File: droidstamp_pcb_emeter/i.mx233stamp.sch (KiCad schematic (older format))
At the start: 0 parts

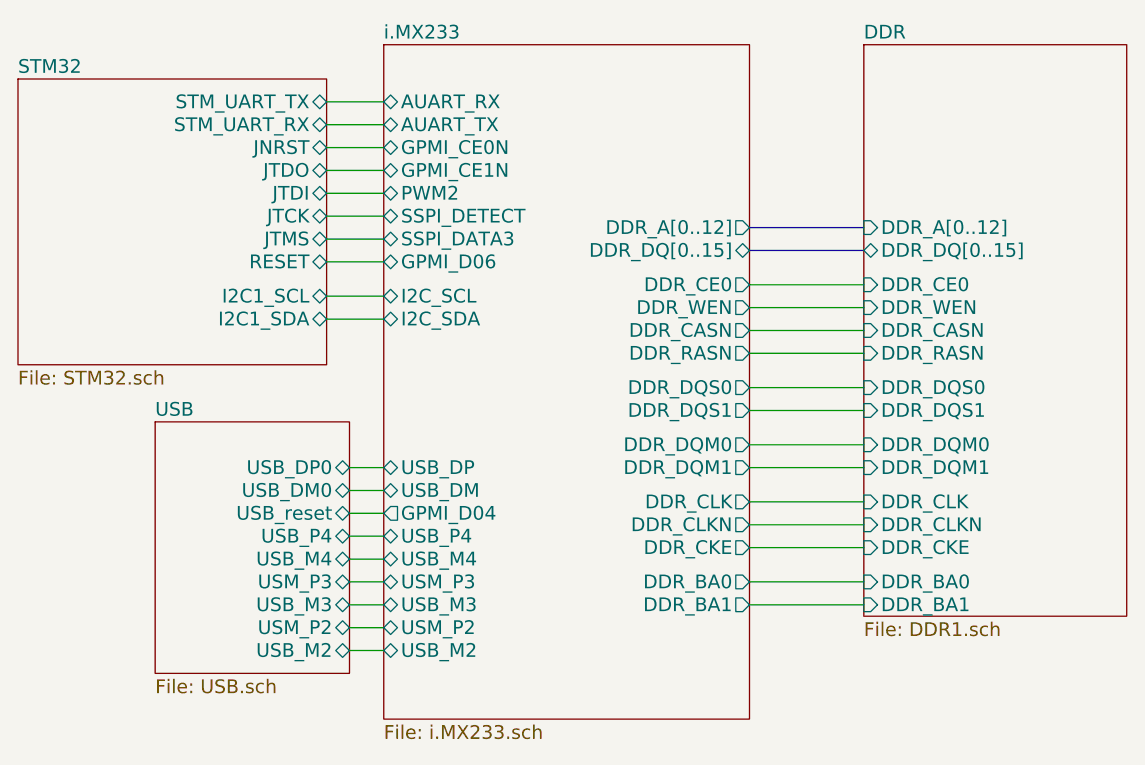
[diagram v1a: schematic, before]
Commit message: Adición de la linea BOOT_MODE para modificar el inicio del stm32 desde memoria interna o jtag
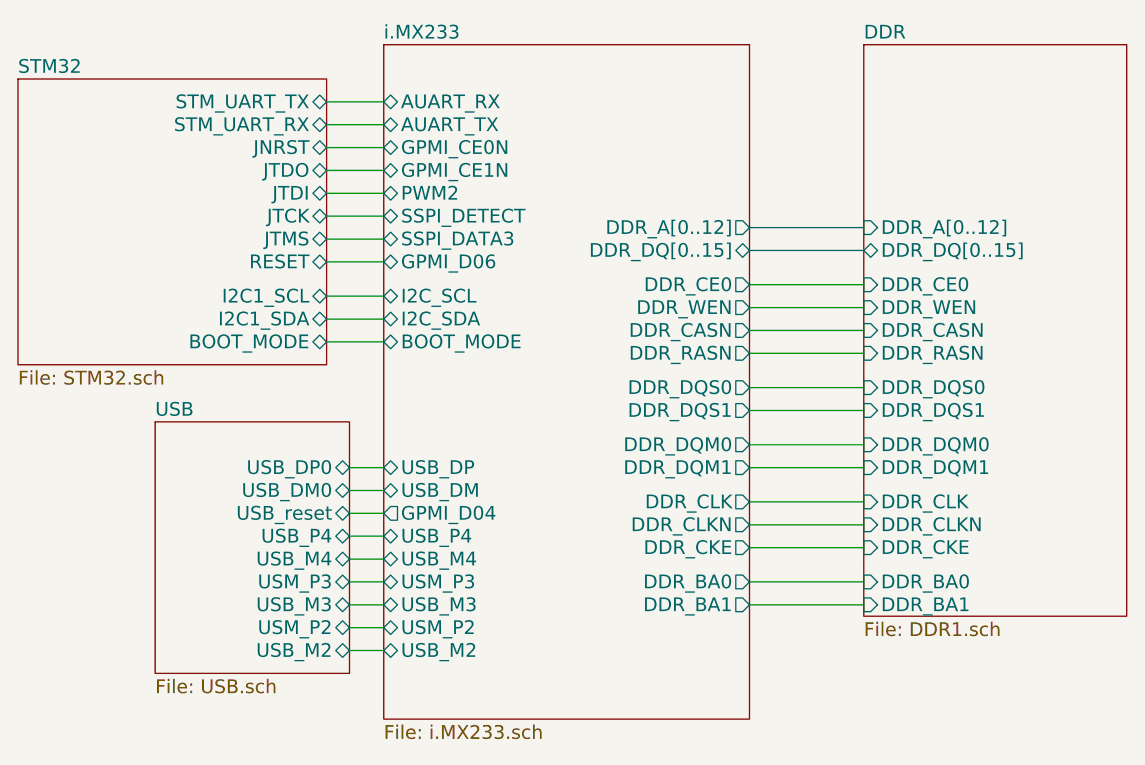
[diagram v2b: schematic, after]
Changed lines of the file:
@@
-EESchema Schematic File Version 2  date vie 20 abr 2012 12:34:33 COT
+EESchema Schematic File Version 2  date Tue 21 Aug 2012 09:23:05 AM COT
 LIBS:con-jack
 LIBS:zxct1009
@@
 Sheet 1 5
 Title ""
-Date "20 apr 2012"
+Date "21 aug 2012"
 Rev ""
 Comp ""
@@
 $EndDescr
 Wire Wire Line
-	3000 3650 3150 3650
-Wire Wire Line
-	2900 1850 3150 1850
-Wire Wire Line
-	2900 2700 3150 2700
-Wire Wire Line
-	3000 4150 3150 4150
-Wire Wire Line
-	2900 2450 3150 2450
-Wire Wire Line
-	2900 2350 3150 2350
-Wire Wire Line
-	2900 2150 3150 2150
-Wire Wire Line
-	3000 3950 3150 3950
-Wire Wire Line
-	3000 3750 3150 3750
-Wire Wire Line
-	3150 3450 3000 3450
+	3150 2900 2900 2900
+Wire Wire Line
+	2900 1950 3150 1950
+Wire Wire Line
+	3150 2800 2900 2800
+Wire Wire Line
+	3000 4250 3150 4250
+Wire Wire Line
+	2900 2550 3150 2550
+Wire Wire Line
+	2900 2250 3150 2250
+Wire Wire Line
+	2900 2050 3150 2050
+Wire Wire Line
+	3000 4050 3150 4050
+Wire Wire Line
+	3000 3850 3150 3850
+Wire Wire Line
+	3000 3550 3150 3550
+Wire Bus Line
+	5250 2400 4750 2400
+Wire Wire Line
+	4750 3450 5250 3450
+Wire Wire Line
+	5250 3200 4750 3200
+Wire Wire Line
+	4750 2950 5250 2950
+Wire Wire Line
+	4750 4050 5250 4050
+Wire Wire Line
+	4750 3800 5250 3800
+Wire Wire Line
+	4750 3600 5250 3600
+Wire Wire Line
+	4750 2850 5250 2850
+Wire Wire Line
+	4750 2750 5250 2750
+Wire Wire Line
+	4750 2650 5250 2650
+Wire Wire Line
+	4750 3700 5250 3700
+Wire Wire Line
+	4750 3950 5250 3950
+Wire Wire Line
+	4750 3100 5250 3100
+Wire Wire Line
+	5250 3350 4750 3350
 Wire Bus Line
 	4750 2500 5250 2500
 Wire Wire Line
-	5250 3350 4750 3350
-Wire Wire Line
-	4750 3100 5250 3100
-Wire Wire Line
-	4750 3950 5250 3950
-Wire Wire Line
-	4750 3700 5250 3700
-Wire Wire Line
-	4750 2650 5250 2650
-Wire Wire Line
-	4750 2750 5250 2750
-Wire Wire Line
-	4750 2850 5250 2850
-Wire Wire Line
-	4750 3600 5250 3600
-Wire Wire Line
-	4750 3800 5250 3800
-Wire Wire Line
-	4750 4050 5250 4050
-Wire Wire Line
-	4750 2950 5250 2950
-Wire Wire Line
-	5250 3200 4750 3200
-Wire Wire Line
-	4750 3450 5250 3450
-Wire Bus Line
-	5250 2400 4750 2400
-Wire Wire Line
-	3000 3550 3150 3550
-Wire Wire Line
-	3000 3850 3150 3850
-Wire Wire Line
-	3000 4050 3150 4050
-Wire Wire Line
-	2900 2050 3150 2050
-Wire Wire Line
-	2900 2250 3150 2250
-Wire Wire Line
-	2900 2550 3150 2550
-Wire Wire Line
-	3000 4250 3150 4250
-Wire Wire Line
-	3150 2800 2900 2800
-Wire Wire Line
-	2900 1950 3150 1950
+	3150 3450 3000 3450
+Wire Wire Line
+	3000 3750 3150 3750
+Wire Wire Line
+	3000 3950 3150 3950
+Wire Wire Line
+	2900 2150 3150 2150
+Wire Wire Line
+	2900 2350 3150 2350
+Wire Wire Line
+	2900 2450 3150 2450
+Wire Wire Line
+	3000 4150 3150 4150
+Wire Wire Line
+	2900 2700 3150 2700
+Wire Wire Line
+	2900 1850 3150 1850
+Wire Wire Line
+	3000 3650 3150 3650
 $Sheet
 S 3150 1600 1600 2950
@@
 F34 "PWM2" B L 3150 2250 60
 F35 "GPMI_D04" O L 3150 3650 60
+F36 "BOOT_MODE" B L 3150 2900 60
 $EndSheet
 $Sheet
@@
 F10 "STM_UART_TX" B R 2900 1850 60
 F11 "STM_UART_RX" B R 2900 1950 60
+F12 "BOOT_MODE" B R 2900 2900 60
 $EndSheet
 $Sheet
